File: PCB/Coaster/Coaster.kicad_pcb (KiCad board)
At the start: 2 copper layers, 198 x 98 mm, 138 parts, among them J1 USB-C, J2 Shelly, J3 Join, P1 TestPoint, P10 TestPoint, P11 TestPoint, P12 TestPoint, P2 TestPoint, P3 TestPoint, P4 TestPoint, P5 TestPoint, P6 TestPoint, P7 TestPoint, P8 TestPoint, P9 TestPoint, T1 TestPoint, T10 TestPoint, T11 TestPoint, T12 TestPoint, T2 TestPoint, T3 TestPoint, T4 TestPoint, T5 TestPoint, T6 TestPoint, T7 TestPoint, T8 TestPoint, T9 TestPoint, U1 ESP32-PICO-MINI-02, U2 LMR16006XDDCR, U3 QR

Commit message: Rotation
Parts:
- turned C1 to -87 degrees
- turned C10 to 138 degrees
- turned C11 to 123 degrees
- turned C12 to 108 degrees
- turned C13 to 93 degrees
- turned C14 to 78 degrees
- turned C15 to 63 degrees
- turned C16 to 48 degrees
- turned C17 to 33 degrees
- turned C18 to 18 degrees
- turned C19 to 3 degrees
- turned C2 to -102 degrees
- turned C20 to -12 degrees
- turned C21 to -27 degrees
- turned C22 to -42 degrees
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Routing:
- net Net-(D10-Pad4): track 8.99 -> 27.0 mm

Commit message: Arrrg
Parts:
- D1, D10, D11, D12, D13, D14, D15, D16, D17, D18, D19, D2, D20, D21, D22, D23, D24, D3, D4, D5, D6, D7, D8, D9: value WS2818B -> WS2812B-2mm
- moved P7 4.00 mm to (110.0, 138.0)
- moved T7 4.00 mm to (190.0, 138.0)
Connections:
- D1 pad 1: VCC -> LED
- D1 pad 2: Net-(D1-Pad2) -> VCC
- D1 pad 3: GND2 -> Net-(D1-Pad3)
- D1 pad 4: LED -> GND2
- D10 pad 1: VCC -> Net-(D10-Pad1)
- D10 pad 2: Net-(D10-Pad2) -> VCC
- D10 pad 3: GND2 -> Net-(D10-Pad3)
- D10 pad 4: Net-(D10-Pad4) -> GND2
- D11 pad 1: VCC -> Net-(D10-Pad3)
- D11 pad 2: Net-(D11-Pad2) -> VCC
- D11 pad 3: GND2 -> Net-(D11-Pad3)
- D11 pad 4: Net-(D10-Pad2) -> GND2
- D12 pad 1: VCC -> Net-(D11-Pad3)
- D12 pad 2: Net-(D12-Pad2) -> VCC
- D12 pad 3: GND2 -> Net-(D13-Pad1)
- D12 pad 4: Net-(D11-Pad2) -> GND2
- D13 pad 1: VCC -> Net-(D13-Pad1)
- D13 pad 2: Net-(D13-Pad2) -> VCC
- D13 pad 3: GND2 -> Net-(D13-Pad3)
- D13 pad 4: Net-(D12-Pad2) -> GND2
- D14 pad 1: VCC -> Net-(D13-Pad3)
- D14 pad 2: Net-(D14-Pad2) -> VCC
- D14 pad 3: GND2 -> Net-(D14-Pad3)
- D14 pad 4: Net-(D13-Pad2) -> GND2
- D15 pad 1: VCC -> Net-(D14-Pad3)
- D15 pad 2: Net-(D15-Pad2) -> VCC
- D15 pad 3: GND2 -> Net-(D15-Pad3)
- D15 pad 4: Net-(D14-Pad2) -> GND2
- D16 pad 1: VCC -> Net-(D15-Pad3)
- D16 pad 2: Net-(D16-Pad2) -> VCC
- D16 pad 3: GND2 -> Net-(D16-Pad3)
- D16 pad 4: Net-(D15-Pad2) -> GND2
- D17 pad 1: VCC -> Net-(D16-Pad3)
- D17 pad 2: Net-(D17-Pad2) -> VCC
- D17 pad 3: GND2 -> Net-(D17-Pad3)
- D17 pad 4: Net-(D16-Pad2) -> GND2
- D18 pad 1: VCC -> Net-(D17-Pad3)
- D18 pad 2: Net-(D18-Pad2) -> VCC
- D18 pad 3: GND2 -> Net-(D18-Pad3)
- D18 pad 4: Net-(D17-Pad2) -> GND2
- D19 pad 1: VCC -> Net-(D18-Pad3)
- D19 pad 2: Net-(D19-Pad2) -> VCC
- D19 pad 3: GND2 -> Net-(D19-Pad3)
- D19 pad 4: Net-(D18-Pad2) -> GND2
- D2 pad 1: VCC -> Net-(D1-Pad3)
- D2 pad 2: Net-(D2-Pad2) -> VCC
- D2 pad 3: GND2 -> Net-(D2-Pad3)
- D2 pad 4: Net-(D1-Pad2) -> GND2
- D20 pad 1: VCC -> Net-(D19-Pad3)
- D20 pad 2: Net-(D20-Pad2) -> VCC
- D20 pad 3: GND2 -> Net-(D20-Pad3)
- D20 pad 4: Net-(D19-Pad2) -> GND2
- D21 pad 1: VCC -> Net-(D20-Pad3)
- D21 pad 2: Net-(D21-Pad2) -> VCC
- D21 pad 3: GND2 -> Net-(D21-Pad3)
- D21 pad 4: Net-(D20-Pad2) -> GND2
- D22 pad 1: VCC -> Net-(D21-Pad3)
- D22 pad 2: Net-(D22-Pad2) -> VCC
- D22 pad 3: GND2 -> Net-(D22-Pad3)
- D22 pad 4: Net-(D21-Pad2) -> GND2
- D23 pad 1: VCC -> Net-(D22-Pad3)
- D23 pad 2: Net-(D23-Pad2) -> VCC
- D23 pad 3: GND2 -> Net-(D23-Pad3)
- D23 pad 4: Net-(D22-Pad2) -> GND2
- D24 pad 1: VCC -> Net-(D23-Pad3)
- D24 pad 2: unconnected-(D24-Pad2) -> VCC
- D24 pad 3: GND2 -> unconnected-(D24-Pad3)
- D24 pad 4: Net-(D23-Pad2) -> GND2
- D3 pad 1: VCC -> Net-(D2-Pad3)
- D3 pad 2: Net-(D3-Pad2) -> VCC
- D3 pad 3: GND2 -> Net-(D3-Pad3)
- D3 pad 4: Net-(D2-Pad2) -> GND2
- D4 pad 1: VCC -> Net-(D3-Pad3)
- D4 pad 2: Net-(D4-Pad2) -> VCC
- D4 pad 3: GND2 -> Net-(D4-Pad3)
- D4 pad 4: Net-(D3-Pad2) -> GND2
- D5 pad 1: VCC -> Net-(D4-Pad3)
- D5 pad 2: Net-(D5-Pad2) -> VCC
- D5 pad 3: GND2 -> Net-(D5-Pad3)
- D5 pad 4: Net-(D4-Pad2) -> GND2
- D6 pad 1: VCC -> Net-(D5-Pad3)
- D6 pad 2: Net-(D6-Pad2) -> VCC
- D6 pad 3: GND2 -> Net-(D6-Pad3)
- D6 pad 4: Net-(D5-Pad2) -> GND2
- D7 pad 1: VCC -> Net-(D6-Pad3)
- D7 pad 2: Net-(D7-Pad2) -> VCC
- D7 pad 3: GND2 -> Net-(D7-Pad3)
- D7 pad 4: Net-(D6-Pad2) -> GND2
- D8 pad 1: VCC -> Net-(D7-Pad3)
- D8 pad 2: Net-(D8-Pad2) -> VCC
- D8 pad 3: GND2 -> Net-(D8-Pad3)
- D8 pad 4: Net-(D7-Pad2) -> GND2
- D9 pad 1: VCC -> Net-(D8-Pad3)
- D9 pad 2: Net-(D10-Pad4) -> VCC
- D9 pad 3: GND2 -> Net-(D10-Pad1)
- D9 pad 4: Net-(D8-Pad2) -> GND2
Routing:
- net Net-(D10-Pad4): track 27.0 -> 0.00 mm
- net Net-(D15-Pad3): track 0.00 -> 8.99 mm
- net Net-(D10-Pad2): track 8.99 -> 0.00 mm
- net Net-(D3-Pad3): track 0.00 -> 8.99 mm
- net Net-(D22-Pad2): track 8.99 -> 0.00 mm
- net Net-(D4-Pad2): track 8.99 -> 0.00 mm
- net Net-(D21-Pad3): track 0.00 -> 8.99 mm
- net Net-(D16-Pad2): track 8.99 -> 0.00 mm
- net Net-(D10-Pad1): track 0.00 -> 8.99 mm
- net Net-(D13-Pad2): track 8.99 -> 0.00 mm
- net Net-(D13-Pad1): track 0.00 -> 8.99 mm
- net Net-(D7-Pad2): track 8.99 -> 0.00 mm
- net Net-(D6-Pad3): track 0.00 -> 8.99 mm
- net Net-(D19-Pad2): track 8.99 -> 0.00 mm
- net Net-(D18-Pad3): track 0.00 -> 8.99 mm
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
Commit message: Orientation
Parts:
- C50: footprint RevK:C_0603_ -> RevK:Hidden
- C51, C52: footprint RevK:C_0805_ -> RevK:Hidden
- D25: footprint RevK:D_1206_ -> RevK:Hidden
- L1: footprint RevK:L_4x4_ -> RevK:Hidden
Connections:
- net +3V3 renamed +3.3V

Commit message: Curvy
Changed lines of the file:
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@@
   (segment (start 93.275 98.55) (end 95.45 98.55) (width 0.25) (layer "F.Cu") (net 43))
   (segment (start 93 98.825) (end 93 100) (width 0.25) (layer "F.Cu") (net 43))
-  (segment (start 106.8 88.5) (end 112.792894 88.5) (width 0.25) (layer "F.Cu") (net 44))
-  (segment (start 105.9 88.2) (end 106.5 88.2) (width 0.25) (layer "F.Cu") (net 44))
-  (segment (start 106.5 88.2) (end 106.8 88.5) (width 0.25) (layer "F.Cu") (net 44))
-  (arc (start 112.792894 88.5) (mid 113.446175 88.370054) (end 114 88) (width 0.25) (layer "F.Cu") (net 44))
+  (segment (start 105.9 88.2) (end 106.217158 88.2) (width 0.25) (layer "F.Cu") (net 44))
+  (segment (start 112.792894 88.5) (end 106.941421 88.5) (width 0.25) (layer "F.Cu") (net 44))
+  (arc (start 106.217158 88.2) (mid 106.47847 88.251979) (end 106.7 88.4) (width 0.25) (layer "F.Cu") (net 44))
+  (arc (start 114 88) (mid 113.446175 88.370054) (end 112.792894 88.5) (width 0.25) (layer "F.Cu") (net 44))
+  (arc (start 106.941421 88.5) (mid 106.810765 88.474011) (end 106.7 88.4) (width 0.25) (layer "F.Cu") (net 44))
   (segment (start 105.9 89) (end 112 89) (width 0.25) (layer "F.Cu") (net 45))
   (arc (start 112 89) (mid 113.414214 89.585786) (end 114 91) (width 0.25) (layer "F.Cu") (net 45))
@@
   (arc (start 104 94.55) (mid 104.131802 94.868198) (end 104.45 95) (width 0.25) (layer "F.Cu") (net 46))
   (arc (start 113 95) (mid 113.707107 94.707107) (end 114 94) (width 0.25) (layer "F.Cu") (net 46))
-  (segment (start 113 123.414213) (end 113 135) (width 0.25) (layer "F.Cu") (net 47))
-  (segment (start 107.425 86.675) (end 114.548833 86.675) (width 0.25) (layer "F.Cu") (net 47))
-  (segment (start 118 90.126167) (end 118 111.343146) (width 0.25) (layer "F.Cu") (net 47))
-  (segment (start 105.9 85.8) (end 106.55 85.8) (width 0.25) (layer "F.Cu") (net 47))
-  (segment (start 106.55 85.8) (end 107.425 86.675) (width 0.25) (layer "F.Cu") (net 47))
-  (arc (start 114 121) (mid 113.259892 122.10765) (end 113 123.414213) (width 0.25) (layer "F.Cu") (net 47))
-  (arc (start 118 111.343146) (mid 116.960434 116.569398) (end 114 121) (width 0.25) (layer "F.Cu") (net 47))
-  (arc (start 114.548833 86.675) (mid 116.989177 87.685823) (end 118 90.126167) (width 0.25) (layer "F.Cu") (net 47))
-  (arc (start 113 135) (mid 112.12132 137.12132) (end 110 138) (width 0.25) (layer "F.Cu") (net 47))
+  (segment (start 113 135) (end 113 123.414213) (width 0.25) (layer "F.Cu") (net 47))
+  (segment (start 106.090381 85.8) (end 105.9 85.8) (width 0.25) (layer "F.Cu") (net 47))
+  (segment (start 107.075 86.325) (end 106.875 86.125) (width 0.25) (layer "F.Cu") (net 47))
+  (segment (start 118 111.343146) (end 118 90.126167) (width 0.25) (layer "F.Cu") (net 47))
+  (segment (start 114.548833 86.675) (end 107.919974 86.675) (width 0.25) (layer "F.Cu") (net 47))
+  (arc (start 107.919974 86.675) (mid 107.462677 86.584038) (end 107.075 86.325) (width 0.25) (layer "F.Cu") (net 47))
+  (arc (start 110 138) (mid 112.12132 137.12132) (end 113 135) (width 0.25) (layer "F.Cu") (net 47))
+  (arc (start 118 90.126167) (mid 116.989177 87.685823) (end 114.548833 86.675) (width 0.25) (layer "F.Cu") (net 47))
+  (arc (start 106.875 86.125) (mid 106.515013 85.884465) (end 106.090381 85.8) (width 0.25) (layer "F.Cu") (net 47))
+  (arc (start 113 123.414213) (mid 113.259892 122.10765) (end 114 121) (width 0.25) (layer "F.Cu") (net 47))
+  (arc (start 114 121) (mid 116.960434 116.569398) (end 118 111.343146) (width 0.25) (layer "F.Cu") (net 47))
   (arc (start 199.51 65.85) (mid 199.21 65.26) (end 198.5 65.03) (width 0.25) (layer "F.Cu") (net 49))
   (arc (start 192.4 65.84) (mid 191.66 65.75) (end 191.22 65.24) (width 0.25) (layer "F.Cu") (net 49))

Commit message: Tweak
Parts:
- C50: footprint RevK:Hidden -> RevK:C_0603_
- C51, C52: footprint RevK:Hidden -> RevK:C_0805_
- D25: footprint RevK:Hidden -> RevK:D_1206_
- L1: footprint RevK:Hidden -> RevK:L_4x4_

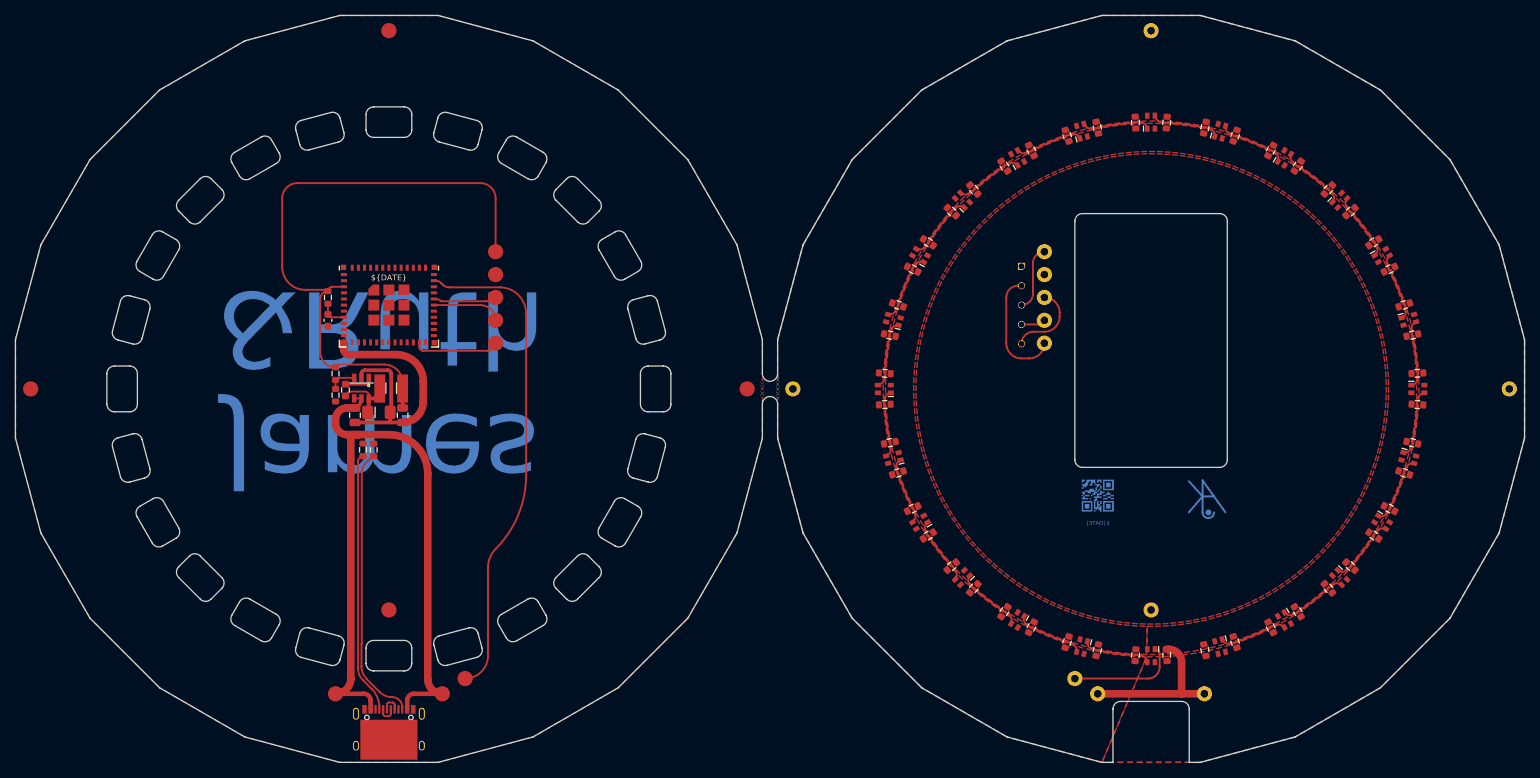
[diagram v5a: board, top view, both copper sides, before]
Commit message: Changed pads for easier soldering next time
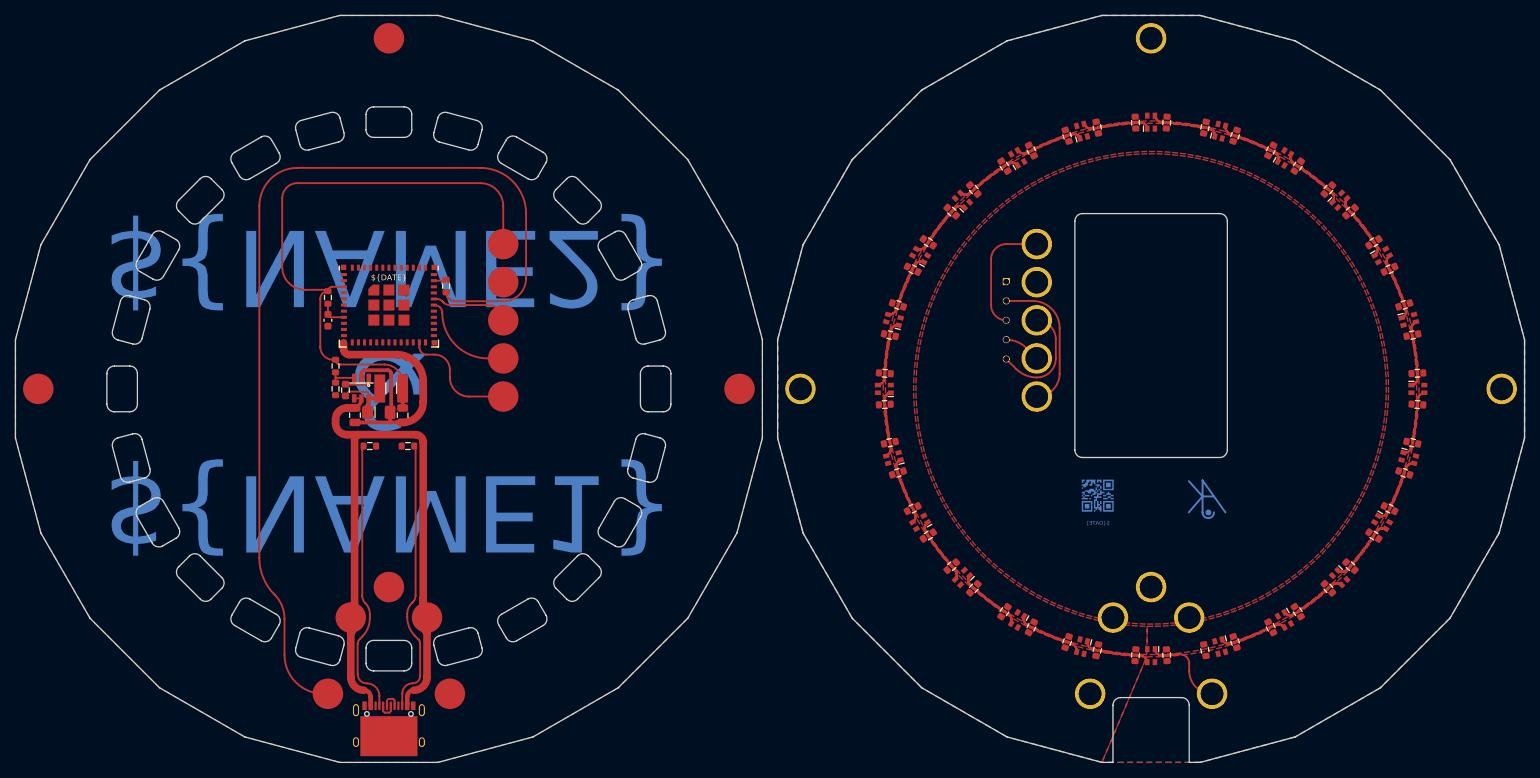
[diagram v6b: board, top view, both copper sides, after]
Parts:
- removed J3: Join, RevK:PCB-Join
- added P13: TestPoint, RevK:PAD, F.Cu at (108.0, 140.0)
- added R6: 30k 1%, RevK:R_0603, F.Cu at (93.0, 100.0)
- added T13: TestPoint, RevK:PAD-LINK, F.Cu at (192.0, 140.0)
- C1, C10, C11, C12, C13, C14, C15, C16, C17, C18, C19, C2, C20, C21, C22, C23, C24, C25, C26, C27, C28, C29, C3, C30, C31, C32, C33, C34, C35, C36, C37, C38, C39, C4, C40, C41, C42, C43, C44, C45, C46, C47, C48, C5, C6, C7, C8, C9: value 10nF -> 100nF
- R4: value 100k 1% -> 300R
- R5: value 30k 1% -> 100k 1%
- moved R4 18.5 mm to (107.5, 86.5)
- moved P7 18.1 mm to (92.0, 140.0)
- moved T7 18.1 mm to (208.0, 140.0)
- moved P1 10.2 mm to (105.0, 130.0)
- moved P2 10.2 mm to (95.0, 130.0)
- moved T1 10.2 mm to (195.0, 130.0)
- moved T2 10.2 mm to (205.0, 130.0)
- moved P6 7.07 mm to (115.0, 101.0)
- moved T6 7.07 mm to (185.0, 101.0)
- moved P4 5.10 mm to (115.0, 96.0)
- moved T4 5.10 mm to (185.0, 96.0)
- moved R3 4.53 mm to (102.5, 107.5), turned to 180 degrees
- moved R5 3.83 mm to (93.0, 97.0), turned to -90 degrees
- moved P3 3.16 mm to (115.0, 91.0)
- moved T3 3.16 mm to (185.0, 91.0)
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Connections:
- R4 pad 1: +3.3V -> Net-(R4-Pad1)
- R4 pad 2: Net-(R4-Pad2) -> Net-(P7-Pad1)
- R5 pad 1: GND -> +3.3V
- R5 pad 2: Net-(R4-Pad2) -> Net-(R5-Pad2)
- U1 pad 34: Net-(P7-Pad1) -> Net-(R4-Pad1)
- U2 pad 3: Net-(R4-Pad2) -> Net-(R5-Pad2)
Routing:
- net Net-(P7-Pad1): track 64.9 -> 129.6 mm
- net Net-(D10-Pad1): track 8.99 -> 71.9 mm
- net Net-(D15-Pad3): track 8.99 -> 45.0 mm
- net Net-(D3-Pad3): track 8.99 -> 45.0 mm
- net Net-(D21-Pad3): track 8.99 -> 45.0 mm
- net Net-(D12-Pad3): track 8.99 -> 44.9 mm
- net Net-(D6-Pad3): track 8.99 -> 44.9 mm
- net Net-(D18-Pad3): track 8.99 -> 44.9 mm
- net Net-(D10-Pad3): track 8.99 -> 44.9 mm
- net Net-(D22-Pad3): track 8.99 -> 44.9 mm
- net Net-(D4-Pad3): track 8.99 -> 44.9 mm
- net Net-(D16-Pad3): track 8.99 -> 44.9 mm
- net Net-(D17-Pad3): track 8.98 -> 44.9 mm
- net Net-(D5-Pad3): track 8.98 -> 44.9 mm
- net Net-(D11-Pad3): track 8.98 -> 44.9 mm
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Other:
- outline, holes or cut-outs redrawn
- board text added: "${NAME1} & ${NAME2}"
- board text removed: "James &Ruth"

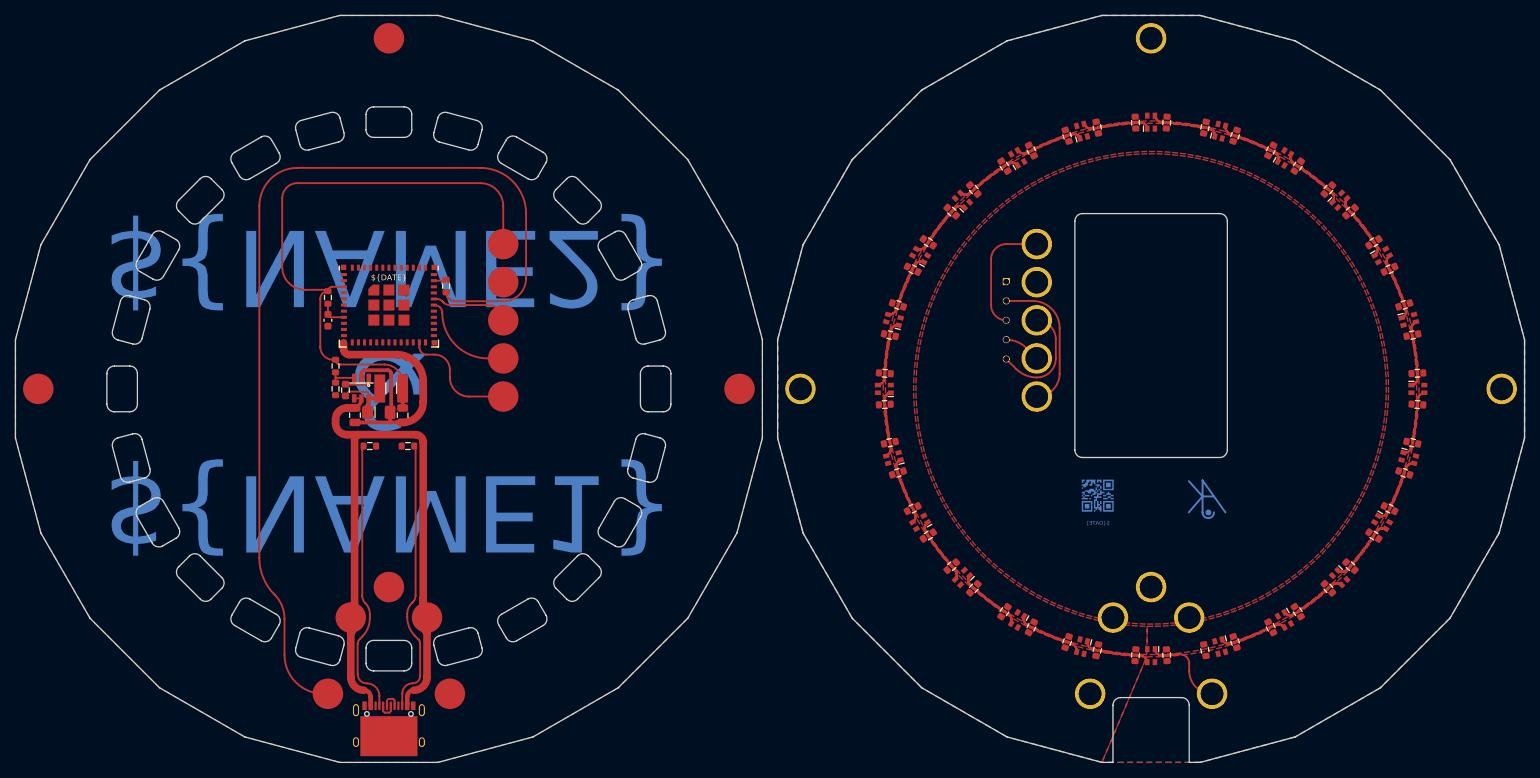
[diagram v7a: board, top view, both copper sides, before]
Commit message: Cleaner DRC
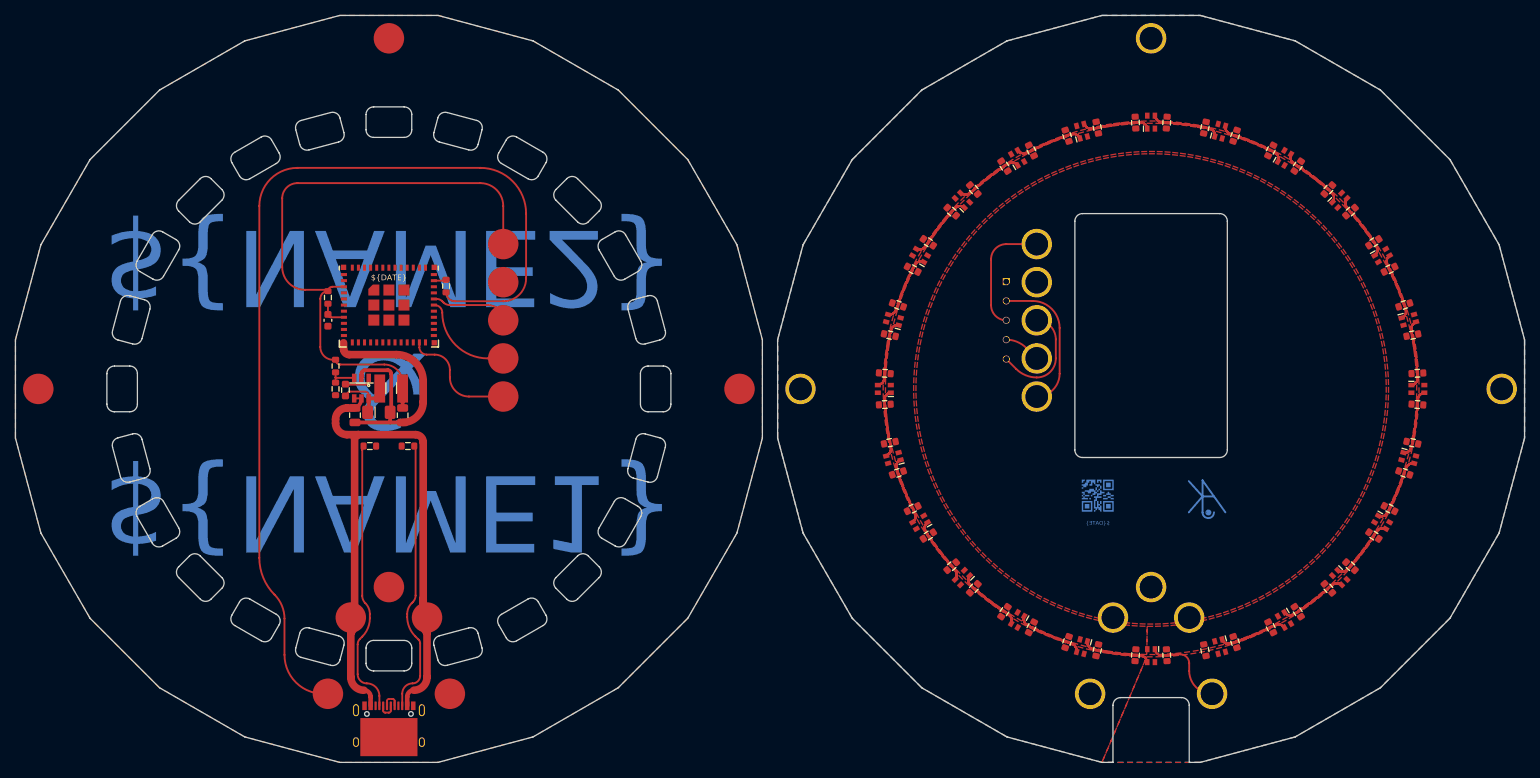
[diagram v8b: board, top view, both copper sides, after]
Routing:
- net Net-(D15-DOUT): track 45.0 -> 71.9 mm
- net Net-(D10-DIN): track 71.9 -> 98.9 mm
- net Net-(D3-DOUT): track 45.0 -> 71.9 mm
- net Net-(D21-DOUT): track 45.0 -> 71.9 mm
- net Net-(D12-DOUT): track 44.9 -> 71.9 mm
- net Net-(D6-DOUT): track 44.9 -> 71.9 mm
- net Net-(D18-DOUT): track 44.9 -> 71.9 mm
- net Net-(D10-DOUT): track 44.9 -> 71.9 mm
- net Net-(D22-DOUT): track 44.9 -> 71.9 mm
- net Net-(D16-DOUT): track 44.9 -> 71.9 mm
- net Net-(D4-DOUT): track 44.9 -> 71.9 mm
- net Net-(D5-DOUT): track 44.9 -> 71.9 mm
- net Net-(D11-DOUT): track 44.9 -> 71.9 mm
- net Net-(D23-DOUT): track 44.9 -> 71.9 mm
- net Net-(D17-DOUT): track 44.9 -> 71.9 mm
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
